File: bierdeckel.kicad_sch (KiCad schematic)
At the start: 28 parts, among them J1 Pogo, J2 Pogo, J6 USB-TYPE-C-020, Q1 BSS138P,215, SW1 PTS526 SK15 SMTR2 LFS, SW2 PTS526 SK15 SMTR2 LFS, SW3 PTS526 SK15 SMTR2 LFS, U1 ESP32-C3-WROOM-02

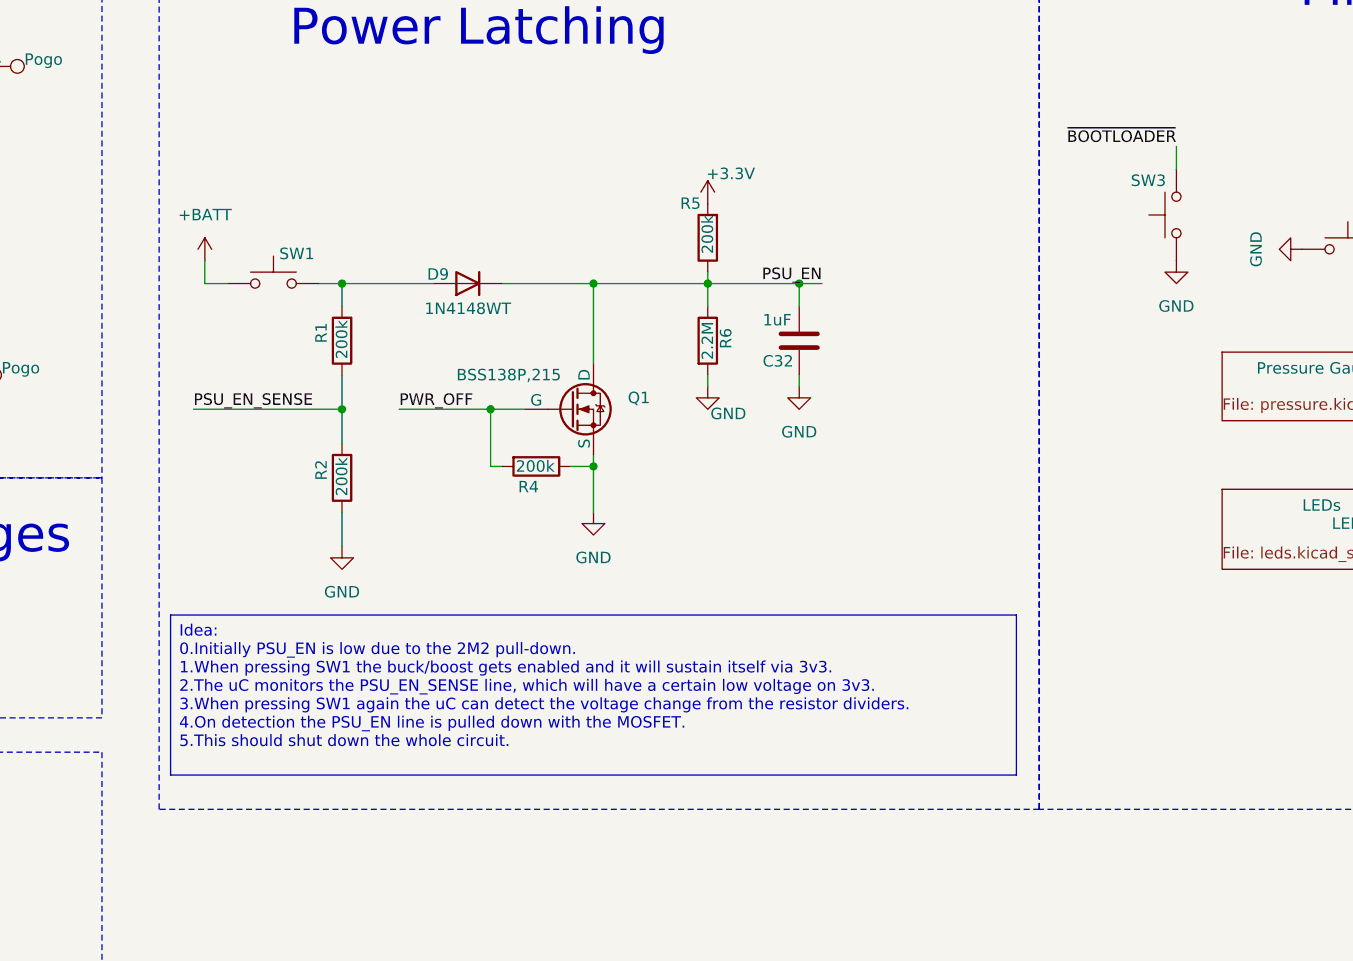
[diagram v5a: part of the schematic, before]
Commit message: add 555 based power latching
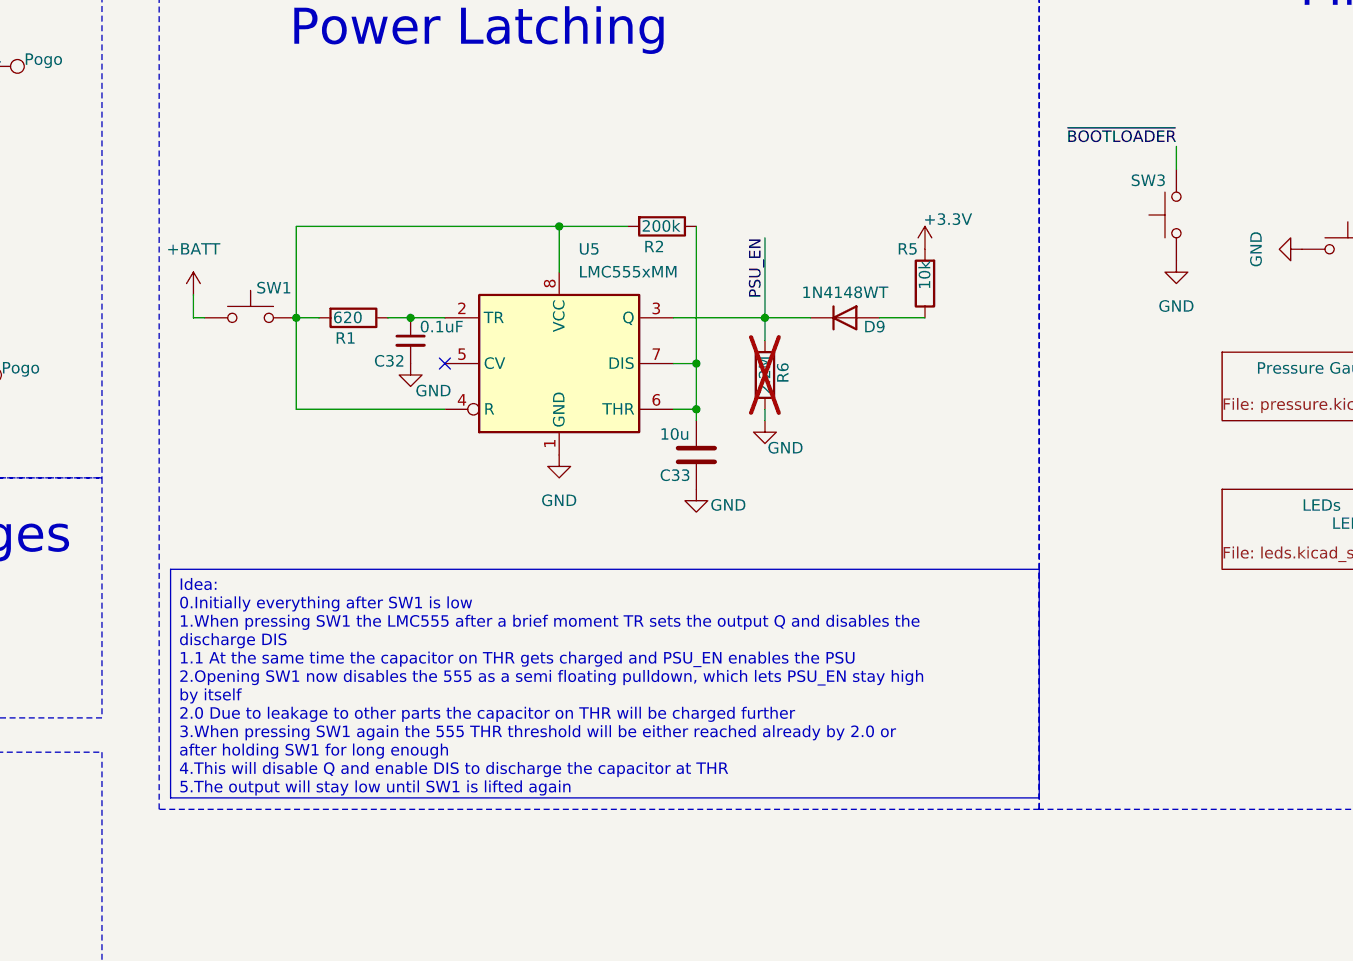
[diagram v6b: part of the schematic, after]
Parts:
- removed Q1: BSS138P,215, Package_TO_SOT_SMD:SOT-23-3, symbol Simulation_SPICE:NMOS
- removed R4: 200k, Resistor_SMD:R_0603_1608Metric, symbol Device:R
- added C33: 10u, Capacitor_SMD:C_0805_2012Metric, symbol Device:C
- added U5: LMC555xMM, Package_SO:VSSOP-8_3x3mm_P0.65mm, symbol Timer:LMC555xMM
- C32: value 1uF -> 0.1uF; symbol Device:C -> Device:C_Small
- R1: value 200k -> 620
- R5: value 200k -> 10k
- R6: now not fitted
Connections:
- net GND: now also C33.2, U5.1 (GND); no longer R2.1
- net PSU_EN: now also U5.3 (Q); no longer C32.1, R5.1
- net PSU_EN_SENSE: no longer R1.1, R2.2
- net at R1.2, SW1.2: now also R2.2, U5.4 (R), U5.8 (VCC); no longer D9.2 (A)
- new net: C32.1, R1.1, U5.2 (TR)
- new net: C33.1, R2.1, U5.6 (THR), U5.7 (DIS)
- new net: D9.2 (A), R5.1
- no-connect marks 7 -> 8
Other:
- moved on the sheet: C32, D9, R1, R2, R5, SW1

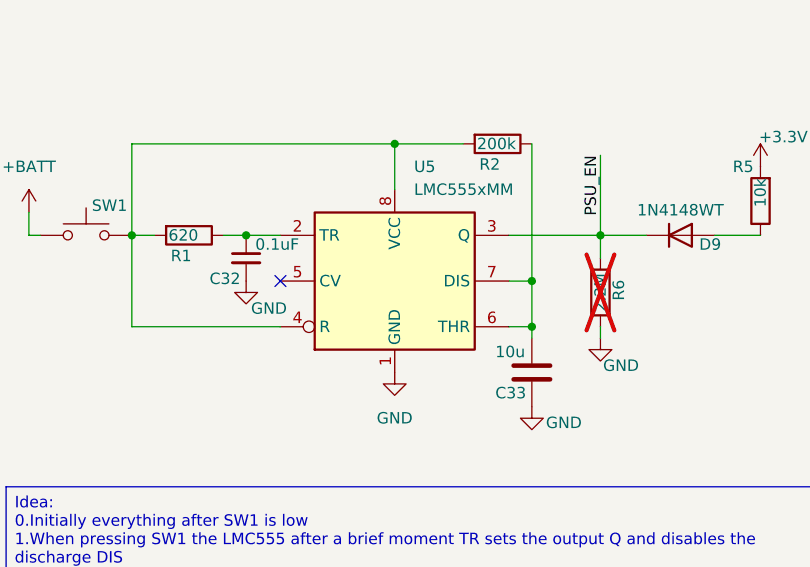
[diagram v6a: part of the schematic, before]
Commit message: route power latch circuit
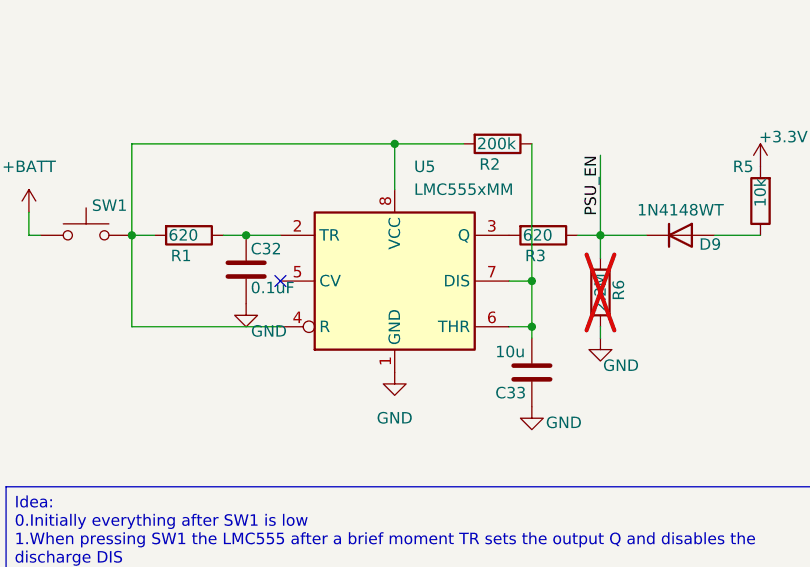
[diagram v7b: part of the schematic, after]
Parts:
- removed C32: 0.1uF, Capacitor_SMD:C_0805_2012Metric, symbol Device:C_Small
- added C32: 0.1uF, Capacitor_SMD:C_0603_1608Metric, symbol Device:C
- added R3: 620, Resistor_SMD:R_0603_1608Metric, symbol Device:R
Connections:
- net GND: now also C32.2
- net PSU_EN: now also R3.1; no longer U5.3 (Q)
- net at R1.1, U5.2 (TR): now also C32.1
- new net: R3.2, U5.3 (Q)
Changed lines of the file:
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@@
 	)
 	(junction
-		(at 115.57 58.42)
+		(at 45.72 50.8)
 		(diameter 0)
 		(color 0 0 0 0)
 	)
 	(junction
-		(at 45.72 50.8)
+		(at 115.57 58.42)
 		(diameter 0)
 		(color 0 0 0 0)
@@
 	(wire
 		(pts
-			(xy 144.78 58.42) (xy 154.94 58.42)
-		)
-		(stroke
-			(width 0)
-			(type default)
-		)
-	)
-	(wire
-		(pts
 			(xy 132.08 48.26) (xy 132.08 53.34)
 		)
@@
 	(wire
 		(pts
+			(xy 152.4 58.42) (xy 154.94 58.42)
+		)
+		(stroke
+			(width 0)
+			(type default)
+		)
+	)
+	(wire
+		(pts
 			(xy 231.14 78.74) (xy 245.11 78.74)
 		)
@@
 	(wire
 		(pts
+			(xy 115.57 58.42) (xy 119.38 58.42)
+		)
+		(stroke
+			(width 0)
+			(type default)
+		)
+	)
+	(wire
+		(pts
 			(xy 44.45 50.8) (xy 45.72 50.8)
 		)
@@
 	(wire
 		(pts
-			(xy 115.57 58.42) (xy 119.38 58.42)
+			(xy 113.03 58.42) (xy 115.57 58.42)
 		)
 		(stroke
@@
 	(wire
 		(pts
-			(xy 113.03 58.42) (xy 115.57 58.42)
-		)
-		(stroke
-			(width 0)
-			(type default)
-		)
-	)
-	(wire
-		(pts
 			(xy 63.5 30.48) (xy 68.58 30.48)
 		)
@@
 	)
 	(symbol
-		(lib_id "Device:C_Small")
-		(at 115.57 60.96 0)
-		(unit 1)
-		(exclude_from_sim no)
-		(in_bom yes)
-		(on_board yes)
-		(dnp no)
-		(property "Reference" "C32"
-			(at 111.506 63.246 0)
-			(effects
-				(font
-					(size 1.27 1.27)
-				)
-				(justify left)
-			)
-		)
-		(property "Value" "0.1uF"
-			(at 116.586 59.436 0)
-			(effects
-				(font
-					(size 1.27 1.27)
-				)
-				(justify left)
-			)
-		)
-		(property "Footprint" "Capacitor_SMD:C_0805_2012Metric"
-			(at 115.57 60.96 0)
-			(effects
-				(font
-					(size 1.27 1.27)
-				)
-				(hide yes)
-			)
-		)
-		(property "Datasheet" "~"
-			(at 115.57 60.96 0)
-			(effects
-				(font
-					(size 1.27 1.27)
-				)
-				(hide yes)
-			)
-		)
-		(property "Description" "Unpolarized capacitor, small symbol"
-			(at 115.57 60.96 0)
-			(effects
-				(font
-					(size 1.27 1.27)
-				)
-				(hide yes)
-			)
-		)
-		(property "mpn" "CL21B105KAFNNNG "
-			(at 115.57 60.96 0)
-			(effects
-				(font
-					(size 1.27 1.27)
-				)
-				(hide yes)
-			)
-		)
-		(pin "1"
-		)
-		(pin "2"
-		)
-		(instances
-			(project "bierdeckel"
-				(path "/a4ffe097-37ef-4e19-a91a-ae57f4a5aad1"
-					(reference "C32")
-					(unit 1)
-				)
-			)
-		)
-	)
-	(symbol
 		(lib_id "power:GND")
 		(at 45.72 86.36 180)
@@
 	(symbol
 		(lib_id "power:GND")
-		(at 115.57 63.5 0)
+		(at 115.57 66.04 0)
 		(unit 1)
 		(exclude_from_sim no)
@@
 		(dnp no)
 		(property "Reference" "#PWR021"
-			(at 115.57 69.85 0)
+			(at 115.57 72.39 0)
 			(effects
 				(font
@@
 		)
 		(property "Value" "GND"
-			(at 118.11 66.548 0)
+			(at 118.11 69.088 0)
 			(effects
 				(font
@@
 		)
 		(property "Footprint" ""
-			(at 115.57 63.5 0)
+			(at 115.57 66.04 0)
 			(effects
 				(font
@@
 		)
 		(property "Datasheet" ""
-			(at 115.57 63.5 0)
+			(at 115.57 66.04 0)
 			(effects
 				(font
@@
 		)
 		(property "Description" "Power symbol creates a global label with name \"GND\" , ground"
-			(at 115.57 63.5 0)
+			(at 115.57 66.04 0)
 			(effects
 				(font
@@
 	)
 	(symbol
+		(lib_id "Device:C")
+		(at 115.57 62.23 0)
+		(unit 1)
+		(exclude_from_sim no)
+		(in_bom yes)
+		(on_board yes)
+		(dnp no)
+		(property "Reference" "C32"
+			(at 116.078 59.944 0)
+			(effects
+				(font
+					(size 1.27 1.27)
+				)
+				(justify left)
+			)
+		)
+		(property "Value" "0.1uF"
+			(at 116.078 64.262 0)
+			(effects
+				(font
+					(size 1.27 1.27)
+				)
+				(justify left)
+			)
+		)
+		(property "Footprint" "Capacitor_SMD:C_0603_1608Metric"
+			(at 116.5352 66.04 0)
+			(effects
+				(font
+					(size 1.27 1.27)
+				)
+				(hide yes)
+			)
+		)
+		(property "Datasheet" "~"
+			(at 115.57 62.23 0)
+			(effects
+				(font
+					(size 1.27 1.27)
+				)
+				(hide yes)
+			)
+		)
+		(property "Description" "Unpolarized capacitor"
+			(at 115.57 62.23 0)
+			(effects
+				(font
+					(size 1.27 1.27)
+				)
+				(hide yes)
+			)
+		)
+		(property "mpn" "KGM21NR71H104KT"
+			(at 115.57 62.23 0)
+			(effects
+				(font
+					(size 1.27 1.27)
+				)
+				(hide yes)
+			)
+		)
+		(pin "1"
+		)
+		(pin "2"
+		)
+		(instances
+			(project "bierdeckel"
+				(path "/a4ffe097-37ef-4e19-a91a-ae57f4a5aad1"
+					(reference "C32")
+					(unit 1)
+				)
+			)
+		)
+	)
+	(symbol
 		(lib_id "Device:R")
 		(at 143.51 48.26 270)
@@
 					(unit 1)
 				)
+			)
+		)
+	)
+	(symbol
+		(lib_id "Device:R")
+		(at 148.59 58.42 270)
+		(unit 1)
+		(exclude_from_sim no)
+		(in_bom yes)
+		(on_board yes)
+		(dnp no)
+		(property "Reference" "R3"
+			(at 146.558 60.706 90)
+			(effects
+				(font
+					(size 1.27 1.27)
+				)
+				(justify left)
+			)
+		)
+		(property "Value" "620"
+			(at 146.304 58.42 90)
+			(effects
+				(font
+					(size 1.27 1.27)
+				)
+				(justify left)
+			)
+		)
+		(property "Footprint" "Resistor_SMD:R_0603_1608Metric"
+			(at 148.59 56.642 90)
+			(effects
+				(font
+					(size 1.27 1.27)
+				)
+				(hide yes)
+			)
+		)
+		(property "Datasheet" "~"
+			(at 148.59 58.42 0)
+			(effects
+				(font
+					(size 1.27 1.27)
+				)
+				(hide yes)
+			)
+		)
+		(property "Description" "Resistor"
+			(at 148.59 58.42 0)
+			(effects
+				(font
+					(size 1.27 1.27)
+				)
+				(hide yes)
+			)
+		)
+		(property "mpn" ""
+			(at 148.59 58.42 0)
+			(effects
+				(font
+					(size 1.27 1.27)
+				)
+				(hide yes)
+			)
+		)
+		(pin "1"
+		)
+		(pin "2"
+		)
+		(instances
+			(project "bierdeckel"
+				(path "/a4ffe097-37ef-4e19-a91a-ae57f4a5aad1"
+					(reference "R3")
+					(unit 1)
+				)

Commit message: prepare for ordering
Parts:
- added R4: 10k, Resistor_SMD:R_0603_1608Metric, symbol Device:R
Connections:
- net GND: now also R4.1
- net at R1.2, R2.2, SW1.2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: now also R4.2
- no-connect marks 8 -> 10
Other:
- moved on the sheet: SW1
